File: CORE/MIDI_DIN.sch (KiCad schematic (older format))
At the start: 60 parts, among them J1 Conn_02x08_Odd_Even, J2 USB_C_Receptacle_USB2.0, J3 Conn_01x04, J5 MAB5100S, J6 MAB5100S, J7 Conn_01x06, Q1 MMBT3906, SW1 SW_SPDT, SW2 SW_Push_DPDT, SW3 PROG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

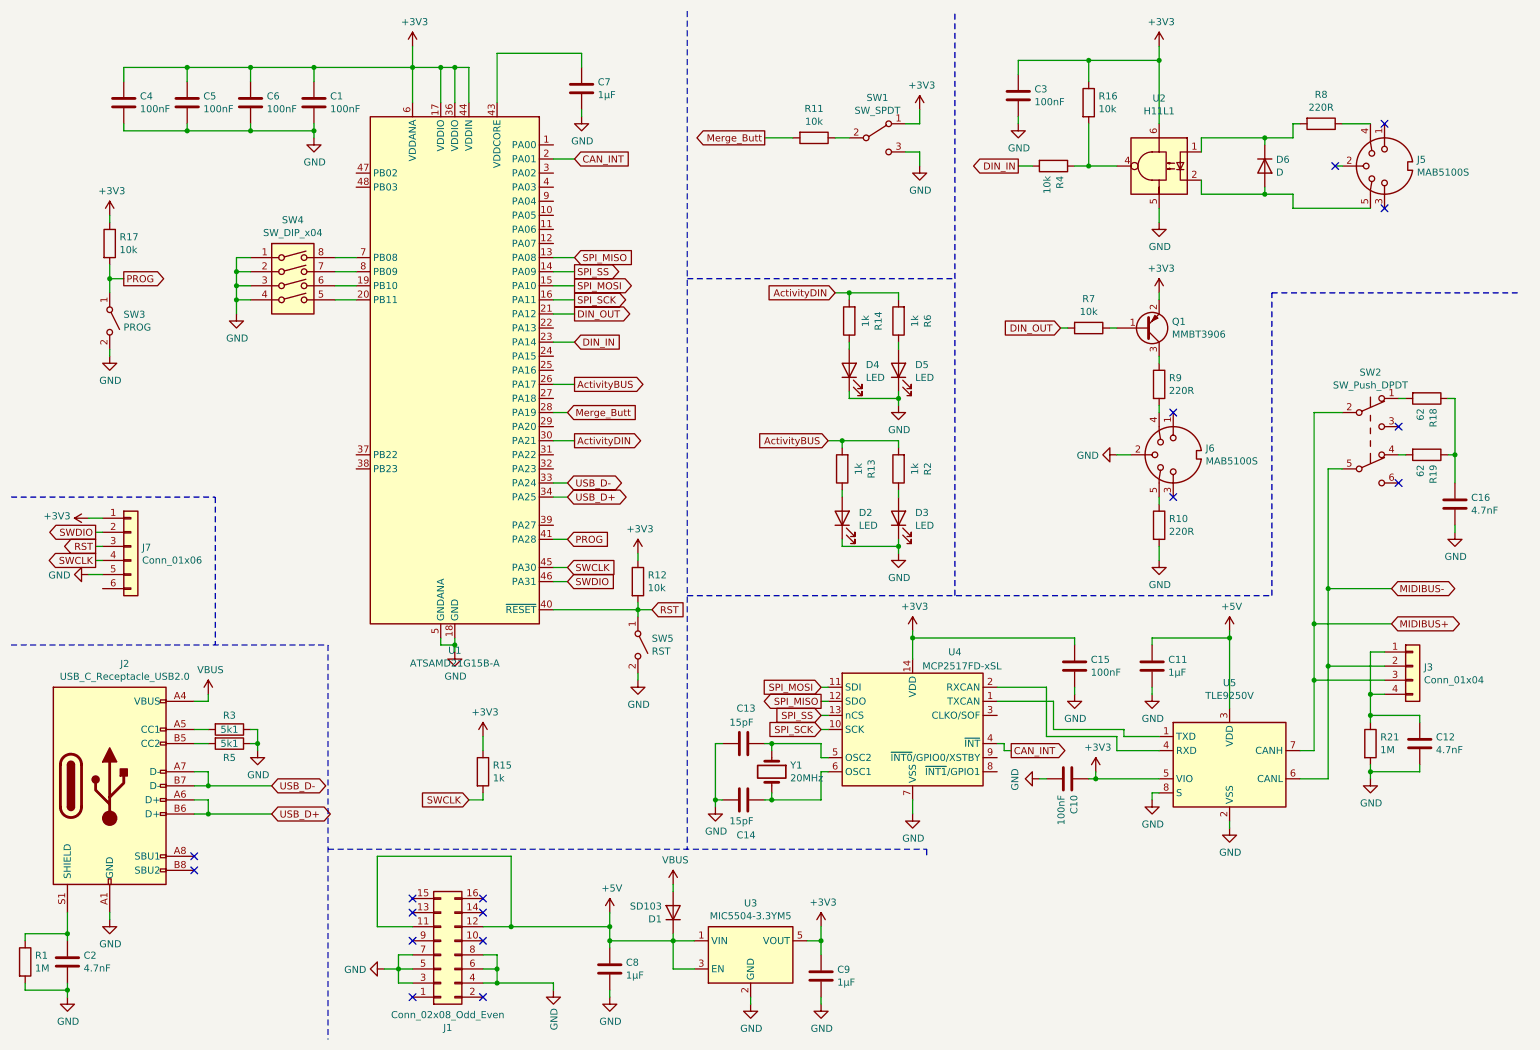
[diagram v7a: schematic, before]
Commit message: Add 5V power protection
Prevent USB connection from powering other modules
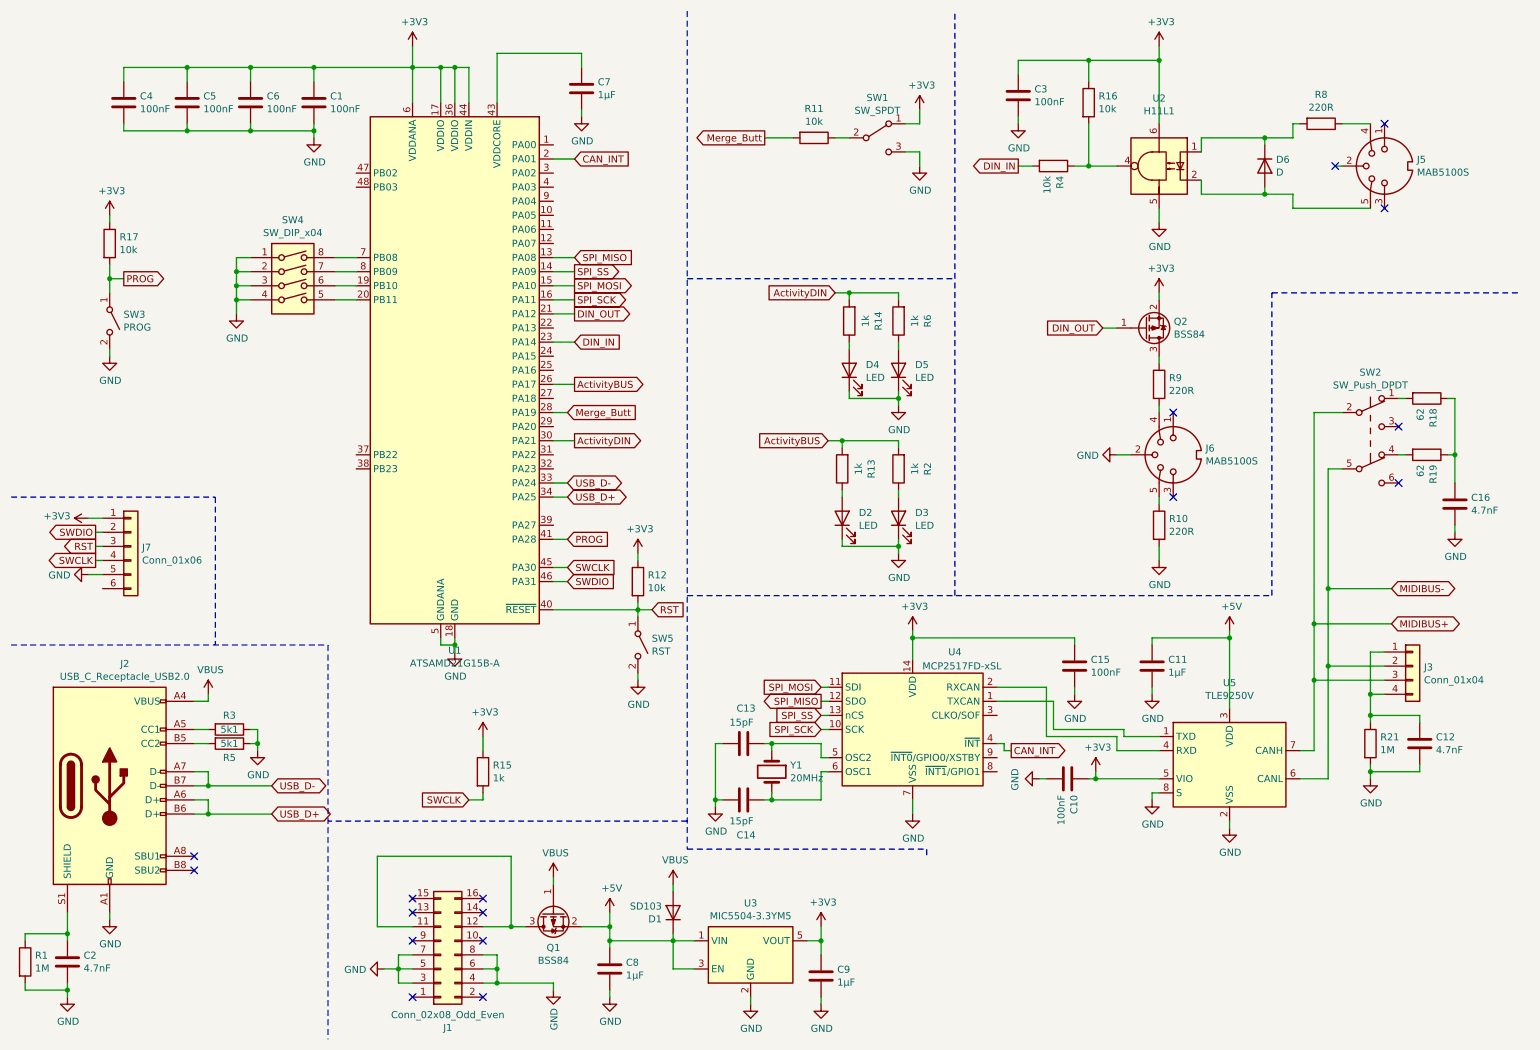
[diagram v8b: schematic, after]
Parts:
- removed Q1: MMBT3906, Package_TO_SOT_SMD:SOT-23, symbol Transistor_BJT:MMBT3906
- removed R7: 10k, Resistor_SMD:R_0603_1608Metric, symbol Device:R
- added Q1, Q2: BSS84, Package_TO_SOT_SMD:SOT-23, symbol Transistor_FET:BSS84
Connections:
- net +3V3: now also Q2.2 (S)
- net +5V: now also Q1.2 (S); no longer J1.11 (Pin_11), J1.12 (Pin_12)
- net DIN_OUT: now also Q2.1 (G)
- net VBUS: now also Q1.1 (G)
- net at R9.1: now also Q2.3 (D)
- new net: J1.11 (Pin_11), J1.12 (Pin_12), Q1.3 (D)
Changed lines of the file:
@@
 Wire Wire Line
 	8650 1900 8650 2000
-Wire Wire Line
-	8350 2750 8300 2750
 $Comp
 L power:GND #PWR0107
@@
 Wire Wire Line
 	7650 1600 7750 1600
-$Comp
-L Device:R R7
-U 1 1 5F6BC9DC
-P 8150 2750
-F 0 "R7" V 7943 2750 50  0000 C CNN
-F 1 "10k" V 8034 2750 50  0000 C CNN
-F 2 "Resistor_SMD:R_0603_1608Metric" V 8080 2750 50  0001 C CNN
-F 3 "~" H 8150 2750 50  0001 C CNN
-	1    8150 2750
-	0    1    1    0
-$EndComp
-Wire Wire Line
-	8000 2750 7950 2750
-Text GLabel 7950 2750 0    50   Input ~ 0
+Text GLabel 8250 2750 0    50   Input ~ 0
 DIN_OUT
 NoConn ~ 10250 1300
@@
 $EndComp
 Wire Wire Line
-	4750 6900 4750 7000
-Wire Wire Line
 	3950 7400 4350 7400
 Wire Wire Line
 	4350 7400 4350 7450
 Connection ~ 3950 7400
-Connection ~ 4050 7000
-Connection ~ 4750 7000
-Wire Wire Line
-	4750 7000 4750 7100
 Wire Wire Line
 	3950 7200 3950 7300
@@
 	8200 5950 8150 5950
 Wire Wire Line
-	4050 7000 4750 7000
-Wire Wire Line
 	3850 7300 3950 7300
 Connection ~ 3950 7300
@@
 	7000 6450 7000 6500
 Wire Notes Line
-	2750 6450 7000 6450
+	5300 6450 7000 6450
 Wire Notes Line
 	5300 500  5300 6450
@@
 	1200 2300 1200 2400
 Connection ~ 1200 2400
-$Comp
-L Transistor_BJT:MMBT3906 Q1
-U 1 1 63C394F5
-P 8550 2750
-F 0 "Q1" H 8741 2704 50  0000 L CNN
-F 1 "MMBT3906" H 8741 2795 50  0000 L CNN
-F 2 "Package_TO_SOT_SMD:SOT-23" H 8750 2675 50  0001 L CIN
-F 3 "https://www.fairchildsemi.com/datasheets/2N/2N3906.pdf" H 8550 2750 50  0001 L CNN
-	1    8550 2750
-	1    0    0    1
-$EndComp
 Wire Wire Line
 	8650 2950 8650 3000
@@
 	10750 3650 10750 3850
 Connection ~ 10750 3650
+$Comp
+L Transistor_FET:BSS84 Q2
+U 1 1 64186328
+P 8550 2750
+F 0 "Q2" H 8754 2704 50  0000 L CNN
+F 1 "BSS84" H 8754 2795 50  0000 L CNN
+F 2 "Package_TO_SOT_SMD:SOT-23" H 8750 2675 50  0001 L CIN
+F 3 "http://assets.nexperia.com/documents/data-sheet/BSS84.pdf" H 8550 2750 50  0001 L CNN
+	1    8550 2750
+	1    0    0    1
+$EndComp
+Wire Wire Line
+	8250 2750 8350 2750
+$Comp
+L Transistor_FET:BSS84 Q1
+U 1 1 641B2AB8
+P 4350 6900
+F 0 "Q1" V 4599 6900 50  0000 C CNN
+F 1 "BSS84" V 4690 6900 50  0000 C CNN
+F 2 "Package_TO_SOT_SMD:SOT-23" H 4550 6825 50  0001 L CIN
+F 3 "http://assets.nexperia.com/documents/data-sheet/BSS84.pdf" H 4350 6900 50  0001 L CNN
+	1    4350 6900
+	0    -1   1    0
+$EndComp
+Wire Wire Line
+	4750 6900 4750 7000
+Wire Wire Line
+	4050 7000 4150 7000
+Connection ~ 4050 7000
+Wire Wire Line
+	4550 7000 4750 7000
+Connection ~ 4750 7000
+Wire Wire Line
+	4750 7000 4750 7100
+Wire Notes Line
+	5300 6250 2750 6250
+$Comp
+L power:VBUS #PWR0142
+U 1 1 6425FC74
+P 4350 6650
+F 0 "#PWR0142" H 4350 6500 50  0001 C CNN
+F 1 "VBUS" H 4365 6823 50  0000 C CNN
+F 2 "" H 4350 6650 50  0001 C CNN
+F 3 "" H 4350 6650 50  0001 C CNN
+	1    4350 6650
+	1    0    0    -1
+$EndComp
+Wire Wire Line
+	4350 6650 4350 6700
 $EndSCHEMATC
